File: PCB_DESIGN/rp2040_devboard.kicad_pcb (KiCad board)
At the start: 2 copper layers, 21 x 51.5 mm, 40 parts, among them J1 USB_C_Receptacle_USB2.0_14P, J2 Conn_01x20, J3 Conn_01x20, J4 Conn_01x03, SW1 SW_Push, U1 RP2040, U3 W25Q128JVS, U4 MCP1700x-330xxTT, Y1 12MHz

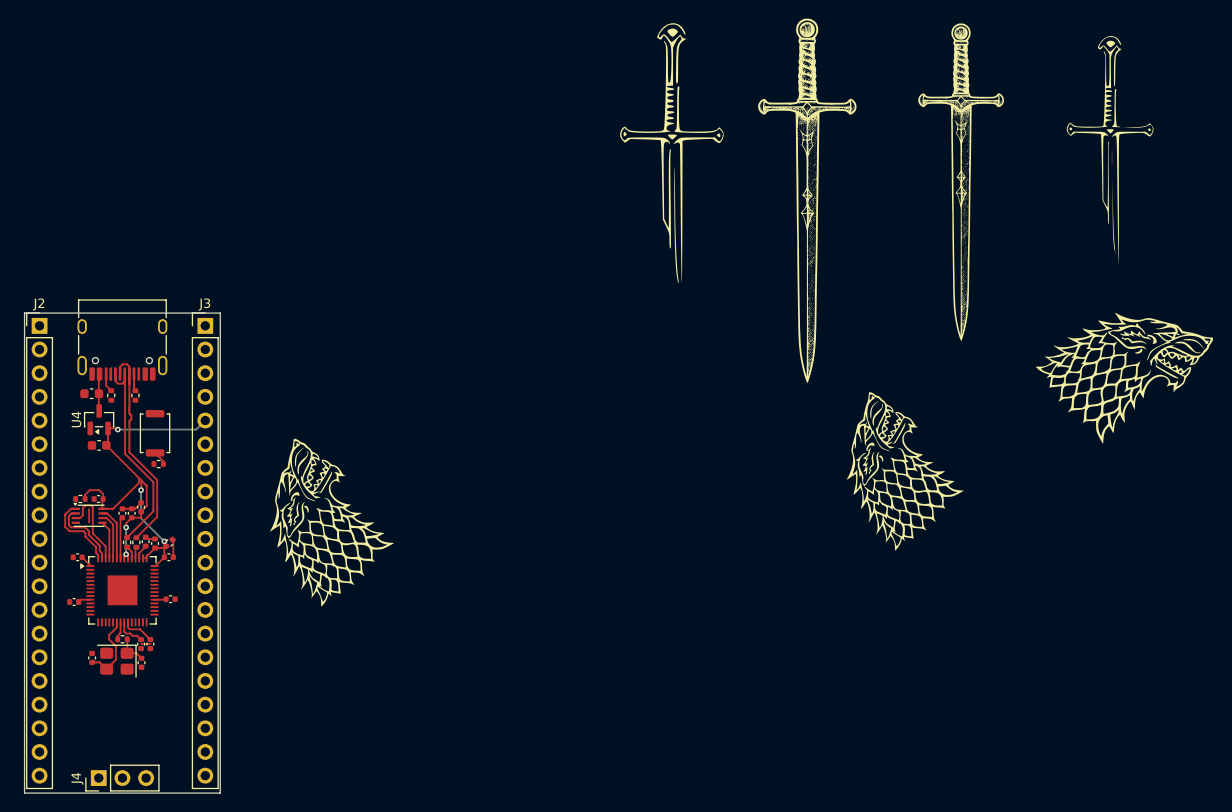
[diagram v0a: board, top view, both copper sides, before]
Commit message: finished routing, fixed drc errors
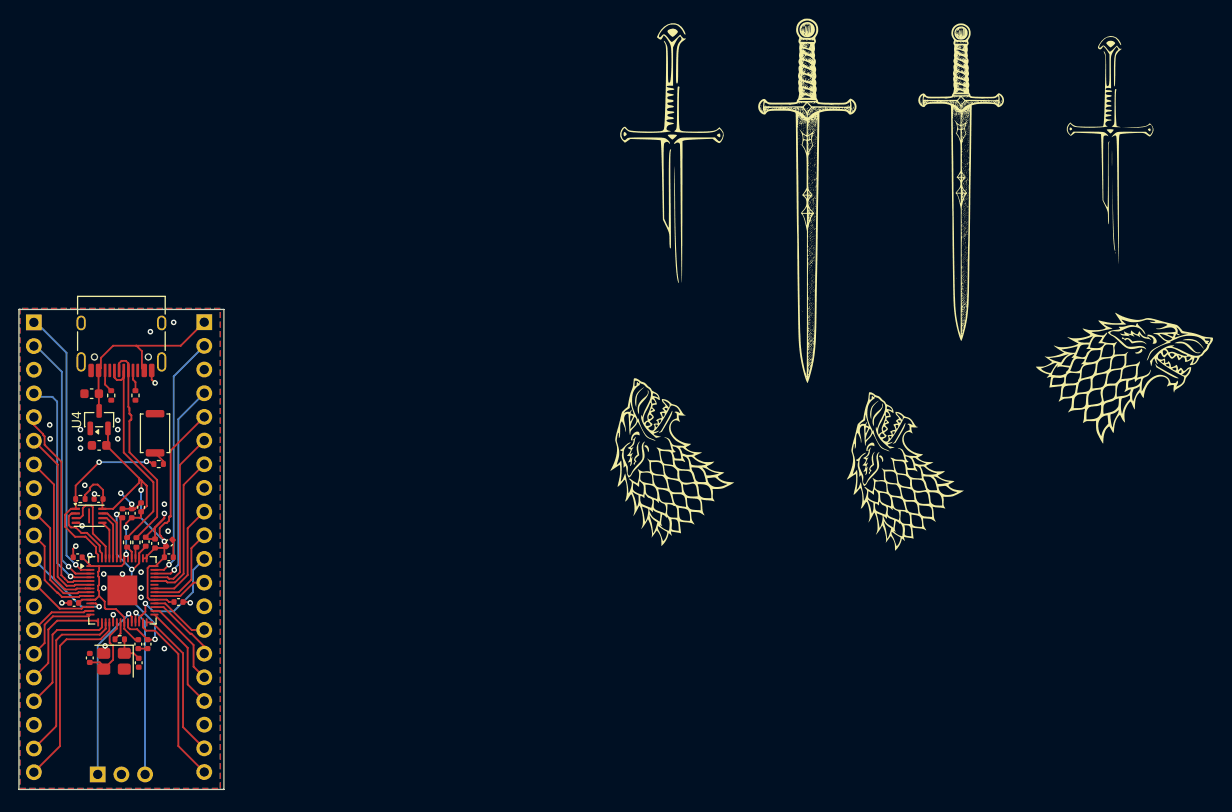
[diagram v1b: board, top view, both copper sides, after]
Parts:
- J2, J3, J4: moved to B.Cu
- moved G*** 37.1 mm to (223.5, 74.0)
- moved C8 0.90 mm to (170.5, 89.0)
- moved J2 0.71 mm to (155.0, 59.0), turned to 180 degrees
- moved J1 0.41 mm to (164.4, 60.1)
- moved J4 0.41 mm to (161.8, 107.5), turned to -90 degrees
- moved J3 0.41 mm to (173.3, 59.0), turned to 180 degrees
- moved C11 0.30 mm to (167.2, 93.5)
- moved C16 0.30 mm to (166.2, 95.5)
- moved C2 0.30 mm to (166.2, 93.5)
- moved Y1 0.30 mm to (163.6, 95.3)
- moved R5 0.30 mm to (164.2, 93.0)
- moved C15 0.25 mm to (161.0, 95.0)
- moved C5 0.10 mm to (159.3, 89.1)
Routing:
- net GPIO0: track 0.00 -> 29.0 mm, vias 0 -> 1
- net GPIO1: track 0.00 -> 27.2 mm, vias 0 -> 1
- net GPIO29_ADC3: track 0.00 -> 26.8 mm, vias 0 -> 1
- net +3V3: track 59.4 -> 83.6 mm, vias 5 -> 4
- net GPIO2: track 0.00 -> 23.7 mm, vias 0 -> 1
- net GPIO28_ADC2: track 0.00 -> 22.6 mm, vias 0 -> 1
- net GPIO3: track 0.00 -> 21.6 mm
- net GPIO15: track 0.00 -> 21.6 mm
- net SWCLK: track 0.00 -> 19.7 mm, vias 0 -> 1
- net GPIO4: track 0.00 -> 19.6 mm
- net GPIO16: track 0.00 -> 19.3 mm
- net GPIO14: track 0.00 -> 19.1 mm
- net SWD: track 0.00 -> 18.8 mm, vias 0 -> 1
- net GPIO27_ADC1: track 0.00 -> 18.3 mm
- net +1V1: track 9.51 -> 27.5 mm, vias 0 -> 3
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- added copper zone on B.Cu, net GND
- added copper zone on F.Cu, net GND
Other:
- board size 21 x 51.5 mm -> 22 x 51.5 mm
